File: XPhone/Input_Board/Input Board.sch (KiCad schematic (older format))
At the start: 92 parts, among them J1 AUDIO, J10 ENV, J11 PULSE, J12 PULSE, J2 AUDIO, J3 ENV, J4 ENV, J5 PULSE, J6 PULSE, J7 AUDIO, J8 AUDIO, J9 ENV, Q1 BC847CW, Q2 BC847CW, Q3 BC847CW, Q4 BC847CW, Q5 BC847CW, Q6 BC847CW, Q7 BC847CW, Q8 BC847CW, U1 LM833, U2 78L05, U3 TL084, U4 74HC14, U5 LM833

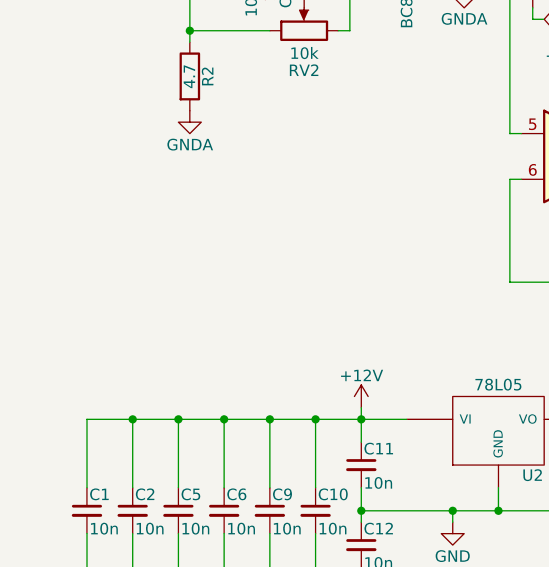
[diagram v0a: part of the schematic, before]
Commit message: XPhone/Input_Board +power connectors
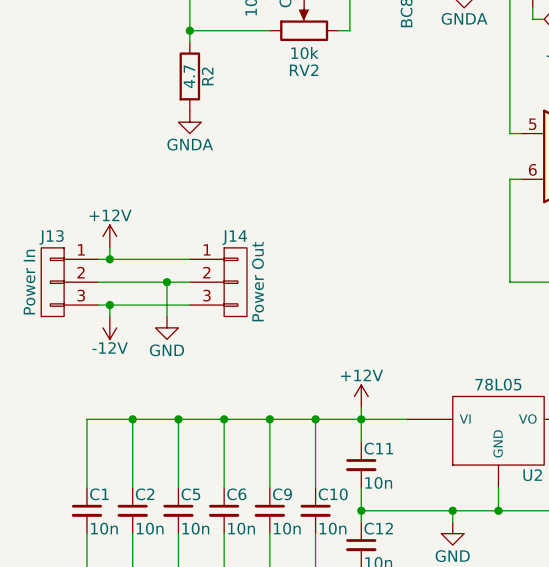
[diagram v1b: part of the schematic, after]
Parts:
- added J13: Power In, Pin_Headers:Pin_Header_Straight_1x03_Pitch2.54mm, symbol CONN_01X03
- added J14: Power Out, Pin_Headers:Pin_Header_Straight_1x03_Pitch2.54mm, symbol CONN_01X03
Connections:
- net +12V: now also J13.1 (P1), J14.1 (P1)
- net -12V: now also J13.3 (P3), J14.3 (P3)
- net GND: now also J13.2 (P2), J14.2 (P2)

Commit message: XPhone/Input_Board
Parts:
- C1, C10, C11, C12, C13, C14, C15, C16, C17, C19, C2, C20, C21, C22, C23, C24, C25, C26, C3, C4, C5, C6, C7, C8, C9: footprint Capacitors_SMD:C_0603 -> Capacitors_SMD:C_0603_HandSoldering
- R1, R10, R11, R12, R13, R14, R15, R16, R17, R18, R19, R2, R20, R21, R22, R23, R24, R25, R26, R27, R28, R29, R3, R30, R31, R32, R33, R4, R5, R6, R7, R8, R9: footprint Resistors_SMD:R_0603 -> Resistors_SMD:R_0603_HandSoldering

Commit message: made tl084 a SOIC and returned 74hc14 back to a DIP
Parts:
- U3: footprint Housings_DIP:DIP-14_W7.62mm -> SMD_Packages:SOIC-14_N
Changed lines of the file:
@@
 F 0 "U3" H 3050 2700 50  0000 L CNN
 F 1 "TL084" H 3050 2300 50  0000 L CNN
-F 2 "Housings_DIP:DIP-14_W7.62mm" H 3000 2600 50  0001 C CNN
+F 2 "SMD_Packages:SOIC-14_N" H 3000 2600 50  0001 C CNN
 F 3 "" H 3100 2700 50  0001 C CNN
 	1    3050 2500
@@
 F 0 "U3" H 8000 2750 50  0000 L CNN
 F 1 "TL084" H 8000 2350 50  0000 L CNN
-F 2 "Housings_DIP:DIP-14_W7.62mm" H 7950 2650 50  0001 C CNN
+F 2 "SMD_Packages:SOIC-14_N" H 7950 2650 50  0001 C CNN
 F 3 "" H 8050 2750 50  0001 C CNN
 	3    8000 2550
@@
 F 0 "U3" H 3050 5450 50  0000 L CNN
 F 1 "TL084" H 3050 5050 50  0000 L CNN
-F 2 "Housings_DIP:DIP-14_W7.62mm" H 3000 5350 50  0001 C CNN
+F 2 "SMD_Packages:SOIC-14_N" H 3000 5350 50  0001 C CNN
 F 3 "" H 3100 5450 50  0001 C CNN
 	2    3050 5250
@@
 F 0 "U3" H 8000 5450 50  0000 L CNN
 F 1 "TL084" H 8000 5050 50  0000 L CNN
-F 2 "Housings_DIP:DIP-14_W7.62mm" H 7950 5350 50  0001 C CNN
+F 2 "SMD_Packages:SOIC-14_N" H 7950 5350 50  0001 C CNN
 F 3 "" H 8050 5450 50  0001 C CNN
 	4    8000 5250

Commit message: XPhone/Input_Board ^layout; using wide TO-92; close to done
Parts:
- U2: footprint TO_SOT_Packages_THT:TO-92_Inline_Narrow_Oval -> TO_SOT_Packages_THT:TO-92_Inline_Wide
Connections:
- net GND: now also U4.11, U4.3
- net at C13.1, C15.2, Q1.3 (C)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: now also U3.5 (+); no longer U3.3 (+)
- net at R16.1: now also U4.5; no longer U4.1
- net at J5.1 (P1): now also U4.6; no longer U4.2
- net at C23.1, C25.2, Q5.3 (C)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: now also U3.12 (+); no longer U3.10 (+)
- net at R32.1: now also U4.13; no longer U4.5
- net at J11.1 (P1): now also U4.12; no longer U4.6
- net at C14.1, C16.2, Q2.3 (C)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: now also U3.3 (+); no longer U3.5 (+)
- net at R17.1: now also U4.1; no longer U4.3
- net at J6.1 (P1): now also U4.2; no longer U4.4
- net at C24.1, C26.2, Q6.3 (C)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: now also U3.10 (+); no longer U3.12 (+)
- new net: J3.1 (P1), U3.6 (-), U3.7
- new net: J9.1 (P1), U3.13 (-), U3.14
- new net: J4.1 (P1), U3.1, U3.2 (-)
- new net: J10.1 (P1), U3.8, U3.9 (-)
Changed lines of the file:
@@
 $Comp
 L 74HC14 U4
-U 1 1 593CBADD
+U 3 1 593CBADD
 P 4350 1750
 F 0 "U4" V 4400 1900 50  0000 C CNN
@@
 F 2 "Housings_DIP:DIP-14_W7.62mm" H 4350 1750 50  0001 C CNN
 F 3 "" H 4350 1750 50  0001 C CNN
-	1    4350 1750
+	3    4350 1750
 	0    1    1    0
 $EndComp
@@
 $Comp
 L TL084 U3
-U 1 1 593CCBBC
+U 2 1 593CCBBC
 P 3050 2500
 F 0 "U3" H 3050 2700 50  0000 L CNN
@@
 F 2 "SMD_Packages:SOIC-14_N" H 3000 2600 50  0001 C CNN
 F 3 "" H 3100 2700 50  0001 C CNN
-	1    3050 2500
+	2    3050 2500
 	1    0    0    -1
 $EndComp
@@
 $Comp
 L 74HC14 U4
-U 3 1 595F1B09
+U 6 1 595F1B09
 P 9300 1800
 F 0 "U4" V 9350 1950 50  0000 C CNN
@@
 F 2 "Housings_DIP:DIP-14_W7.62mm" H 9300 1800 50  0001 C CNN
 F 3 "" H 9300 1800 50  0001 C CNN
-	3    9300 1800
+	6    9300 1800
 	0    1    1    0
 $EndComp
@@
 $Comp
 L TL084 U3
-U 3 1 595F1B2B
+U 4 1 595F1B2B
 P 8000 2550
 F 0 "U3" H 8000 2750 50  0000 L CNN
@@
 F 2 "SMD_Packages:SOIC-14_N" H 7950 2650 50  0001 C CNN
 F 3 "" H 8050 2750 50  0001 C CNN
-	3    8000 2550
+	4    8000 2550
 	1    0    0    -1
 $EndComp
@@
 $Comp
 L 74HC14 U4
-U 2 1 595F219F
+U 1 1 595F219F
 P 4350 4500
 F 0 "U4" V 4400 4650 50  0000 C CNN
@@
 F 2 "Housings_DIP:DIP-14_W7.62mm" H 4350 4500 50  0001 C CNN
 F 3 "" H 4350 4500 50  0001 C CNN
-	2    4350 4500
+	1    4350 4500
 	0    1    1    0
 $EndComp
@@
 $Comp
 L TL084 U3
-U 2 1 595F21C1
+U 1 1 595F21C1
 P 3050 5250
 F 0 "U3" H 3050 5450 50  0000 L CNN
@@
 F 2 "SMD_Packages:SOIC-14_N" H 3000 5350 50  0001 C CNN
 F 3 "" H 3100 5450 50  0001 C CNN
-	2    3050 5250
+	1    3050 5250
 	1    0    0    -1
 $EndComp
@@
 $Comp
 L TL084 U3
-U 4 1 595F3B03
+U 3 1 595F3B03
 P 8000 5250
 F 0 "U3" H 8000 5450 50  0000 L CNN
@@
 F 2 "SMD_Packages:SOIC-14_N" H 7950 5350 50  0001 C CNN
 F 3 "" H 8050 5450 50  0001 C CNN
-	4    8000 5250
+	3    8000 5250
 	1    0    0    -1
 $EndComp
@@
 $Comp
 L 74HC14 U4
-U 5 1 5961DDC6
+U 2 1 5961DDC6
 P 9400 6000
 F 0 "U4" V 9450 6150 50  0000 C CNN
@@
 F 2 "Housings_DIP:DIP-14_W7.62mm" H 9400 6000 50  0001 C CNN
 F 3 "" H 9400 6000 50  0001 C CNN
-	5    9400 6000
+	2    9400 6000
 	0    1    1    0
 $EndComp
 $Comp
 L 74HC14 U4
-U 6 1 5961E25D
+U 5 1 5961E25D
 P 9900 6000
 F 0 "U4" V 9950 6150 50  0000 C CNN
@@
 F 2 "Housings_DIP:DIP-14_W7.62mm" H 9900 6000 50  0001 C CNN
 F 3 "" H 9900 6000 50  0001 C CNN
-	6    9900 6000
+	5    9900 6000
 	0    1    1    0
 $EndComp
@@
 F 0 "U2" H 2800 6254 50  0000 C CNN
 F 1 "78L05" H 2650 6650 50  0000 C CNN
-F 2 "TO_SOT_Packages_THT:TO-92_Inline_Narrow_Oval" H 2650 6450 50  0001 C CNN
+F 2 "TO_SOT_Packages_THT:TO-92_Inline_Wide" H 2650 6450 50  0001 C CNN
 F 3 "" H 2650 6450 50  0001 C CNN
 	1    2650 6450
@@
 Connection ~ 950  5700
 $Comp
-L -12V #PWR?
+L -12V #PWR036
 U 1 1 5970A812
 P 1550 1450
-F 0 "#PWR?" H 1550 1600 50  0001 C CNN
+F 0 "#PWR036" H 1550 1600 50  0001 C CNN
 F 1 "-12V" H 1550 1310 50  0000 C CNN
 F 2 "" H 1550 1450 50  0001 C CNN
@@
 $EndComp
 $Comp
-L -12V #PWR?
+L -12V #PWR037
 U 1 1 5970B2B4
 P 2950 2800
-F 0 "#PWR?" H 2950 2950 50  0001 C CNN
+F 0 "#PWR037" H 2950 2950 50  0001 C CNN
 F 1 "-12V" H 2950 2660 50  0000 C CNN
 F 2 "" H 2950 2800 50  0001 C CNN
@@
 $EndComp
 $Comp
-L -12V #PWR?
+L -12V #PWR038
 U 1 1 5970B597
 P 1550 4200
-F 0 "#PWR?" H 1550 4350 50  0001 C CNN
+F 0 "#PWR038" H 1550 4350 50  0001 C CNN
 F 1 "-12V" H 1550 4060 50  0000 C CNN
 F 2 "" H 1550 4200 50  0001 C CNN
@@
 $EndComp
 $Comp
-L -12V #PWR?
+L -12V #PWR039
 U 1 1 5970C16A
 P 2950 5550
-F 0 "#PWR?" H 2950 5700 50  0001 C CNN
+F 0 "#PWR039" H 2950 5700 50  0001 C CNN
 F 1 "-12V" H 2950 5410 50  0000 C CNN
 F 2 "" H 2950 5550 50  0001 C CNN
@@
 $EndComp
 $Comp
-L -12V #PWR?
+L -12V #PWR040
 U 1 1 5970C2AD
 P 2050 7200
-F 0 "#PWR?" H 2050 7350 50  0001 C CNN
+F 0 "#PWR040" H 2050 7350 50  0001 C CNN
 F 1 "-12V" H 2050 7060 50  0000 C CNN
 F 2 "" H 2050 7200 50  0001 C CNN
@@
 $EndComp
 $Comp
-L -12V #PWR?
+L -12V #PWR041
 U 1 1 5970C798
 P 950 5950
-F 0 "#PWR?" H 950 6100 50  0001 C CNN
+F 0 "#PWR041" H 950 6100 50  0001 C CNN
 F 1 "-12V" H 950 5810 50  0000 C CNN
 F 2 "" H 950 5950 50  0001 C CNN
@@
 $EndComp
 $Comp
-L -12V #PWR?
+L -12V #PWR042
 U 1 1 5970C8DB
 P 6500 4200
-F 0 "#PWR?" H 6500 4350 50  0001 C CNN
+F 0 "#PWR042" H 6500 4350 50  0001 C CNN
 F 1 "-12V" H 6500 4060 50  0000 C CNN
 F 2 "" H 6500 4200 50  0001 C CNN
@@
 $EndComp
 $Comp
-L -12V #PWR?
+L -12V #PWR043
 U 1 1 5970D23E
 P 7900 5550
-F 0 "#PWR?" H 7900 5700 50  0001 C CNN
+F 0 "#PWR043" H 7900 5700 50  0001 C CNN
 F 1 "-12V" H 7900 5410 50  0000 C CNN
 F 2 "" H 7900 5550 50  0001 C CNN
@@
 $EndComp
 $Comp
-L -12V #PWR?
+L -12V #PWR044
 U 1 1 5970D521
 P 7900 2850
-F 0 "#PWR?" H 7900 3000 50  0001 C CNN
+F 0 "#PWR044" H 7900 3000 50  0001 C CNN
 F 1 "-12V" H 7900 2710 50  0000 C CNN
 F 2 "" H 7900 2850 50  0001 C CNN
@@
 $EndComp
 $Comp
-L -12V #PWR?
+L -12V #PWR045
 U 1 1 5970D804
 P 6500 1500
-F 0 "#PWR?" H 6500 1650 50  0001 C CNN
+F 0 "#PWR045" H 6500 1650 50  0001 C CNN
 F 1 "-12V" H 6500 1360 50  0000 C CNN
 F 2 "" H 6500 1500 50  0001 C CNN
@@
 	1    0    0    -1
 $EndComp
+Wire Wire Line
+	9400 5550 9400 5500
+Wire Wire Line
+	9000 5500 9900 5500
+Wire Wire Line
+	9900 5500 9900 5550
+Wire Wire Line
+	9000 5500 9000 5550
+Connection ~ 9400 5500
+$Comp
+L GND #PWR046
+U 1 1 5970EE5A
+P 9000 5550
+F 0 "#PWR046" H 9000 5300 50  0001 C CNN
+F 1 "GND" H 9000 5400 50  0000 C CNN
+F 2 "" H 9000 5550 50  0001 C CNN
+F 3 "" H 9000 5550 50  0001 C CNN
+	1    9000 5550
+	1    0    0    -1
+$EndComp

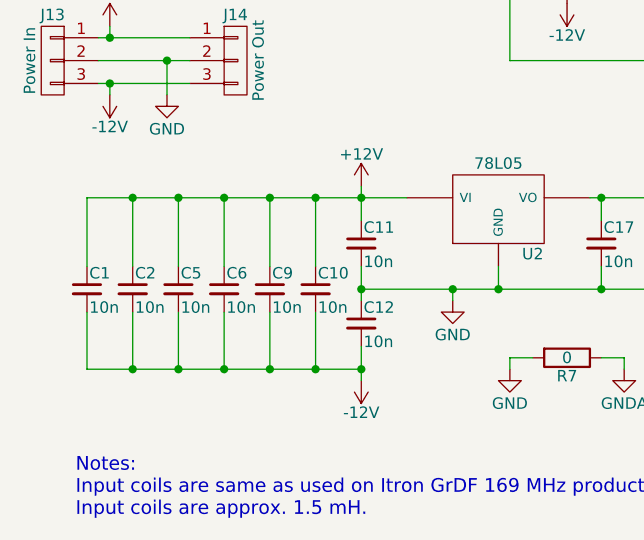
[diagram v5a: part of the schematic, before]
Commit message: XPhone/Input_Board removing unnecessary caps
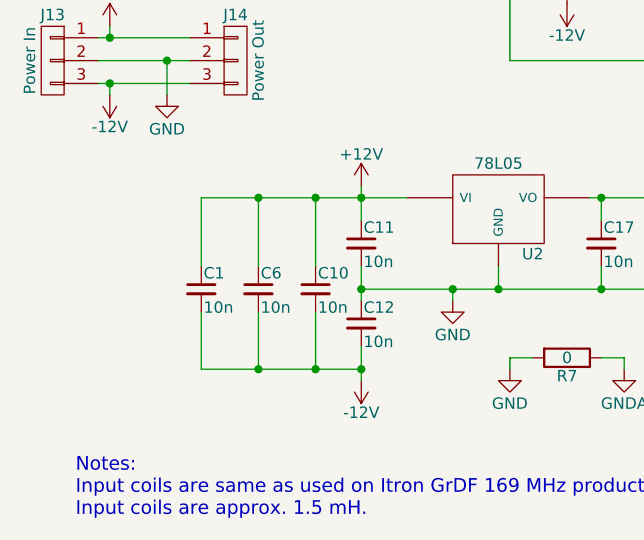
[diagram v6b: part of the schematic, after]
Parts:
- removed C2, C5, C9: 10n, Capacitors_SMD:C_0603_HandSoldering, symbol C_Small
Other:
- moved on the sheet: C1, C6
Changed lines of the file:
@@
 L C_Small C1
 U 1 1 5960E627
-P 850 6800
-F 0 "C1" H 860 6870 50  0000 L CNN
-F 1 "10n" H 860 6720 50  0000 L CNN
-F 2 "Capacitors_SMD:C_0603_HandSoldering" H 850 6800 50  0001 C CNN
-F 3 "" H 850 6800 50  0001 C CNN
-	1    850  6800
-	1    0    0    -1
-$EndComp
-$Comp
-L C_Small C2
-U 1 1 5960E62D
-P 1050 6800
-F 0 "C2" H 1060 6870 50  0000 L CNN
-F 1 "10n" H 1060 6720 50  0000 L CNN
-F 2 "Capacitors_SMD:C_0603_HandSoldering" H 1050 6800 50  0001 C CNN
-F 3 "" H 1050 6800 50  0001 C CNN
-	1    1050 6800
-	1    0    0    -1
-$EndComp
-$Comp
-L C_Small C5
-U 1 1 5960E633
-P 1250 6800
-F 0 "C5" H 1260 6870 50  0000 L CNN
-F 1 "10n" H 1260 6720 50  0000 L CNN
-F 2 "Capacitors_SMD:C_0603_HandSoldering" H 1250 6800 50  0001 C CNN
-F 3 "" H 1250 6800 50  0001 C CNN
-	1    1250 6800
+P 1350 6800
+F 0 "C1" H 1360 6870 50  0000 L CNN
+F 1 "10n" H 1360 6720 50  0000 L CNN
+F 2 "Capacitors_SMD:C_0603_HandSoldering" H 1350 6800 50  0001 C CNN
+F 3 "" H 1350 6800 50  0001 C CNN
+	1    1350 6800
 	1    0    0    -1
 $EndComp
@@
 L C_Small C6
 U 1 1 5960E639
-P 1450 6800
-F 0 "C6" H 1460 6870 50  0000 L CNN
-F 1 "10n" H 1460 6720 50  0000 L CNN
-F 2 "Capacitors_SMD:C_0603_HandSoldering" H 1450 6800 50  0001 C CNN
-F 3 "" H 1450 6800 50  0001 C CNN
-	1    1450 6800
+P 1600 6800
+F 0 "C6" H 1610 6870 50  0000 L CNN
+F 1 "10n" H 1610 6720 50  0000 L CNN
+F 2 "Capacitors_SMD:C_0603_HandSoldering" H 1600 6800 50  0001 C CNN
+F 3 "" H 1600 6800 50  0001 C CNN
+	1    1600 6800
 	1    0    0    -1
 $EndComp
 Wire Wire Line
-	850  6400 850  6700
+	1350 6400 1350 6700
 Wire Wire Line
-	1250 6400 1250 6700
+	1350 6900 1350 7150
 Wire Wire Line
-	1050 6400 1050 6700
+	1600 7150 1600 6900
 Wire Wire Line
-	1050 6900 1050 7150
-Wire Wire Line
-	850  6900 850  7150
-Wire Wire Line
-	1250 7150 1250 6900
-Wire Wire Line
-	1450 7150 1450 6900
-Wire Wire Line
-	1450 6400 1450 6700
-$Comp
-L C_Small C9
-U 1 1 5960E64D
-P 1650 6800
-F 0 "C9" H 1660 6870 50  0000 L CNN
-F 1 "10n" H 1660 6720 50  0000 L CNN
-F 2 "Capacitors_SMD:C_0603_HandSoldering" H 1650 6800 50  0001 C CNN
-F 3 "" H 1650 6800 50  0001 C CNN
-	1    1650 6800
-	1    0    0    -1
-$EndComp
+	1600 6400 1600 6700
 $Comp
 L C_Small C10
@@
 	1850 7150 1850 6900
 Wire Wire Line
-	1650 7150 1650 6900
-Wire Wire Line
 	1850 6400 1850 6700
-Wire Wire Line
-	1650 6400 1650 6700
 Connection ~ 2050 6800
 Wire Wire Line
-	850  6400 2250 6400
-Connection ~ 1050 6400
-Connection ~ 1250 6400
-Connection ~ 1450 6400
-Connection ~ 1650 6400
+	1350 6400 2250 6400
+Connection ~ 1600 6400
 Connection ~ 1850 6400
 Wire Wire Line
-	850  7150 2050 7150
+	1350 7150 2050 7150
 Connection ~ 1850 7150
-Connection ~ 1050 7150
-Connection ~ 1250 7150
-Connection ~ 1450 7150
-Connection ~ 1650 7150
+Connection ~ 1600 7150
 $Comp
 L 74HC14 U4

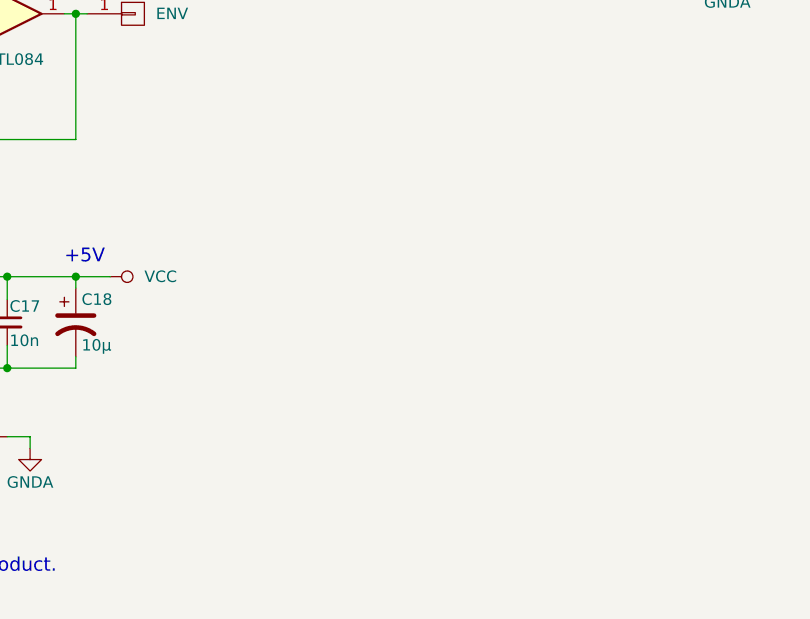
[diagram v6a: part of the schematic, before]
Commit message: XPhone/Input_Board +ENV_BIAS to circuit
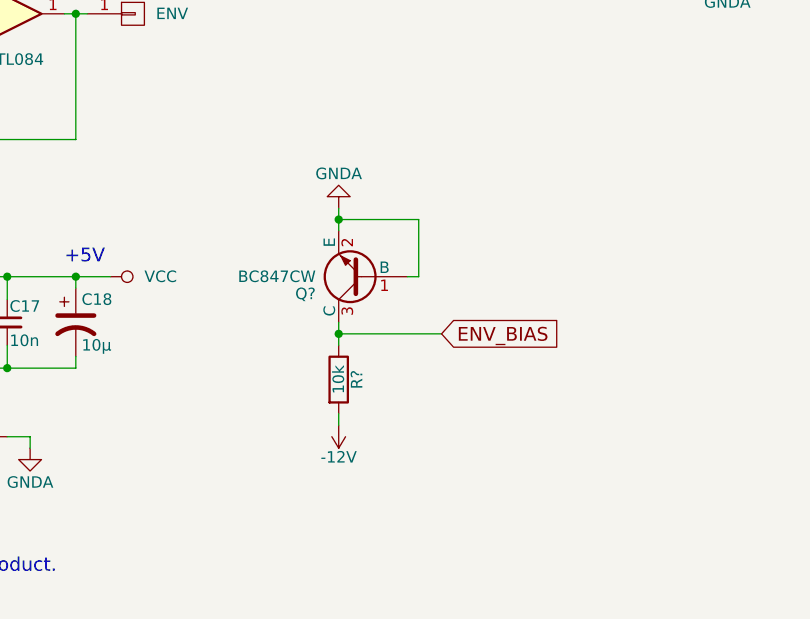
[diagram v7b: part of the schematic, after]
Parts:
- added Q?: BC847CW, TO_SOT_Packages_SMD:SOT-323_SC-70_Handsoldering, symbol MMBT3904
- added R?: 10k, Resistors_SMD:R_0603_HandSoldering, symbol R
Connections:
- net -12V: now also R?.2
- net GNDA: now also Q?.1 (B), Q?.2 (E)
- new net ENV_BIAS: Q?.3 (C), R?.1
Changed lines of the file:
@@
 	1    0    0    -1
 $EndComp
+$Comp
+L MMBT3904 Q?
+U 1 1 59730C4C
+P 4650 6400
+F 0 "Q?" H 4850 6475 50  0000 L CNN
+F 1 "BC847CW" H 4850 6400 50  0000 L CNN
+F 2 "TO_SOT_Packages_SMD:SOT-323_SC-70_Handsoldering" H 4850 6325 50  0001 L CIN
+F 3 "" H 4650 6400 50  0001 L CNN
+	1    4650 6400
+	-1   0    0    1
+$EndComp
+$Comp
+L R R?
+U 1 1 597315BA
+P 4550 6850
+F 0 "R?" V 4630 6850 50  0000 C CNN
+F 1 "10k" V 4550 6850 50  0000 C CNN
+F 2 "Resistors_SMD:R_0603_HandSoldering" V 4480 6850 50  0001 C CNN
+F 3 "" H 4550 6850 50  0001 C CNN
+	1    4550 6850
+	1    0    0    -1
+$EndComp
+$Comp
+L GNDA #PWR?
+U 1 1 59731C7E
+P 4550 6100
+F 0 "#PWR?" H 4550 5850 50  0001 C CNN
+F 1 "GNDA" H 4550 5950 50  0000 C CNN
+F 2 "" H 4550 6100 50  0001 C CNN
+F 3 "" H 4550 6100 50  0001 C CNN
+	1    4550 6100
+	-1   0    0    1
+$EndComp
+Wire Wire Line
+	4850 6400 4900 6400
+Wire Wire Line
+	4900 6400 4900 6150
+Wire Wire Line
+	4900 6150 4550 6150
+Wire Wire Line
+	4550 6100 4550 6200
+Connection ~ 4550 6150
+Wire Wire Line
+	4550 6700 4550 6600
+Wire Wire Line
+	4550 7000 4550 7050
+$Comp
+L -12V #PWR?
+U 1 1 59732F54
+P 4550 7050
+F 0 "#PWR?" H 4550 7200 50  0001 C CNN
+F 1 "-12V" H 4550 6910 50  0000 C CNN
+F 2 "" H 4550 7050 50  0001 C CNN
+F 3 "" H 4550 7050 50  0001 C CNN
+	1    4550 7050
+	1    0    0    -1
+$EndComp
+Wire Wire Line
+	4550 6650 5000 6650
+Connection ~ 4550 6650
+Text GLabel 5000 6650 2    60   Input ~ 0
+ENV_BIAS
 $EndSCHEMATC

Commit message: V_ENV_BIAS
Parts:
- gave numbers to parts that had none: 2
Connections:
- net ENV_BIAS is gone; now on net V_ENV_BIAS: Q9.3 (C), R34.1
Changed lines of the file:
@@
 $EndComp
 $Comp
-L MMBT3904 Q?
+L MMBT3904 Q9
 U 1 1 59730C4C
 P 4650 6400
-F 0 "Q?" H 4850 6475 50  0000 L CNN
+F 0 "Q9" H 4850 6475 50  0000 L CNN
 F 1 "BC847CW" H 4850 6400 50  0000 L CNN
 F 2 "TO_SOT_Packages_SMD:SOT-323_SC-70_Handsoldering" H 4850 6325 50  0001 L CIN
@@
 $EndComp
 $Comp
-L R R?
+L R R34
 U 1 1 597315BA
 P 4550 6850
-F 0 "R?" V 4630 6850 50  0000 C CNN
+F 0 "R34" V 4630 6850 50  0000 C CNN
 F 1 "10k" V 4550 6850 50  0000 C CNN
 F 2 "Resistors_SMD:R_0603_HandSoldering" V 4480 6850 50  0001 C CNN
@@
 $EndComp
 $Comp
-L GNDA #PWR?
+L GNDA #PWR047
 U 1 1 59731C7E
 P 4550 6100
-F 0 "#PWR?" H 4550 5850 50  0001 C CNN
+F 0 "#PWR047" H 4550 5850 50  0001 C CNN
 F 1 "GNDA" H 4550 5950 50  0000 C CNN
 F 2 "" H 4550 6100 50  0001 C CNN
@@
 	4550 7000 4550 7050
 $Comp
-L -12V #PWR?
+L -12V #PWR048
 U 1 1 59732F54
 P 4550 7050
-F 0 "#PWR?" H 4550 7200 50  0001 C CNN
+F 0 "#PWR048" H 4550 7200 50  0001 C CNN
 F 1 "-12V" H 4550 6910 50  0000 C CNN
 F 2 "" H 4550 7050 50  0001 C CNN
@@
 Connection ~ 4550 6650
 Text GLabel 5000 6650 2    60   Input ~ 0
-ENV_BIAS
+V_ENV_BIAS
 $EndSCHEMATC
